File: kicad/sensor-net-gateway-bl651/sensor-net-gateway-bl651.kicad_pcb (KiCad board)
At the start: 2 copper layers, 26 x 56 mm, 41 parts, among them M1 M50-3130545, M2 M50-3130545, SW1 PTS526_SM15_SMTR2_LFS, U1 USB_micro_ab, U2 USBLC6-2SC6, U3 FT230XQ, Y1 32.768 kHz

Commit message: routing snapshot
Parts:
- removed CD1: CORTEX-DEBUG, HH_CNCTech:CORTEX-DEBUG
- added C17: 0.1µF, Capacitor_SMD:C_0603_1608Metric, B.Cu at (154.0, 92.0)
- added L3: logo, HH_Hochreiner:logo, B.Cu at (168.0, 119.0)
- moved LED1 27.3 mm to (174.0, 122.0), turned to 90 degrees
- moved R3 20.7 mm to (173.1, 117.3), turned to 270 degrees
- moved R4 20.4 mm to (174.9, 117.3), turned to 270 degrees
- moved R6 16.8 mm to (159.5, 94.4)
- moved S2 16.6 mm to (154.0, 92.0), turned to 180 degrees
- moved R5 16.0 mm to (159.5, 92.8)
- moved M2 5.60 mm to (156.3, 103.5)
- moved SC1 5.30 mm to (161.4, 87.7)
- moved H2 5.10 mm to (155.0, 85.0)
- moved C14 4.90 mm to (162.4, 96.2)
- moved Y1 4.90 mm to (159.9, 97.8)
- moved BL1 4.81 mm to (169.0, 99.6)
- moved C15 4.80 mm to (156.9, 96.5)
- moved C16 4.80 mm to (156.9, 99.1)
- moved C13 4.64 mm to (172.7, 109.9), turned to 0 degrees
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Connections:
- net Net-(U1-Pad2) renamed /usb/D_N
- net Net-(U1-Pad3) renamed /usb/D_P
- BL1 pad 12: /mcu/FTDI_DIO0 -> /mcu/FTDI_DIO1
- BL1 pad 13: /mcu/FTDI_DIO1 -> /mcu/FTDI_DIO0
- BL1 pad 14: /mcu/FTDI_DIO2 -> /mcu/FTDI_DIO3
- BL1 pad 15: /mcu/FTDI_DIO3 -> /mcu/FTDI_DIO2
- BL1 pad 2: /mcu/SPI_MISO -> /mcu/LED_GREEN
- BL1 pad 21: (no net) -> /mcu/UART2.TX
- BL1 pad 22: (no net) -> /mcu/UART2.RX
- BL1 pad 28: (no net) -> /sensor/SCL
- BL1 pad 3: /mcu/SPI_MOSI -> /mcu/LED_RED
- BL1 pad 30: /sensor/SCL -> /mcu/GPIO_2
- BL1 pad 31: /mcu/LED_GREEN -> /mcu/~SPI_CS
- BL1 pad 32: /mcu/LED_RED -> /mcu/SPI_CLK
- BL1 pad 33: /mcu/GPIO_2 -> /mcu/SPI_MOSI
- BL1 pad 34: /mcu/GPIO_1 -> /mcu/SPI_MISO
- BL1 pad 35: /mcu/~SPI_CS -> /mcu/I2C_SDA
- BL1 pad 37: /mcu/I2C_SDA -> /mcu/GPIO_1
- BL1 pad 38: /mcu/SPI_CLK -> (no net)
- C1 pad 2: /power/GND -> GND
- C10 pad 2: /power/GND -> GND
- C11 pad 2: /power/GND -> GND
- C12 pad 2: /power/GND -> GND
- C2 pad 2: /power/GND -> GND
- C21 pad 2: /power/GND -> GND
- C3 pad 2: /power/GND -> GND
- C4 pad 2: /power/GND -> GND
- C5 pad 2: /power/GND -> GND
- C6 pad 1: /power/GND -> GND
- C7 pad 2: /power/GND -> GND
- C9 pad 2: /power/GND -> GND
- L2 pad 2: /power/GND -> GND
- M2 pad 1: /usb/UART.RX -> /power/3V0
- M2 pad 2: /usb/UART.TX -> /mcu/SWO
- M2 pad 4: /usb/UART.RTS -> /mcu/UART2.TX
- M2 pad 5: /usb/UART.CTS -> /mcu/UART2.RX
- S1 pad 6: /power/GND -> GND
- S1 pad 8: /power/GND -> GND
- S2 pad 4: /power/GND -> GND
- U1 pad 5: /power/GND -> GND
- U2 pad 2: /power/GND -> GND
- U3 pad 13: /power/GND -> GND
- U3 pad 17: /power/GND -> GND
- U3 pad 3: /power/GND -> GND
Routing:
- net /power/3V0: track 0.00 -> 77.7 mm, vias 0 -> 7
- net GND: track 0.00 -> 39.1 mm, vias 0 -> 19
- net /power/VBUS: track 0.00 -> 26.3 mm, vias 0 -> 4
- net /mcu/FTDI_DIO2: track 0.00 -> 21.3 mm, vias 0 -> 2
- net /mcu/GPIO_1: track 0.00 -> 21.3 mm, vias 0 -> 2
- net /usb/UART.CTS: track 0.00 -> 19.7 mm
- net /mcu/I2C_SCL: track 0.00 -> 19.1 mm
- net /mcu/I2C_SDA: track 0.00 -> 17.1 mm
- net /mcu/SWO: track 0.00 -> 17.1 mm, vias 0 -> 2
- net /usb/UART.RX: track 0.00 -> 17.0 mm
- net /mcu/~RESET: track 0.00 -> 14.7 mm, vias 0 -> 1
- net /mcu/FTDI_DIO3: track 0.00 -> 14.1 mm, vias 0 -> 2
- net /mcu/SWDIO: track 0.00 -> 14.1 mm, vias 0 -> 2
- net /usb/UART.RTS: track 0.00 -> 13.0 mm
- net /mcu/FTDI_DIO1: track 0.00 -> 13.0 mm
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- added copper zone on B.Cu, net GND
- added copper zone on F.Cu, net GND
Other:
- board size 26 x 56 mm -> 24 x 50 mm

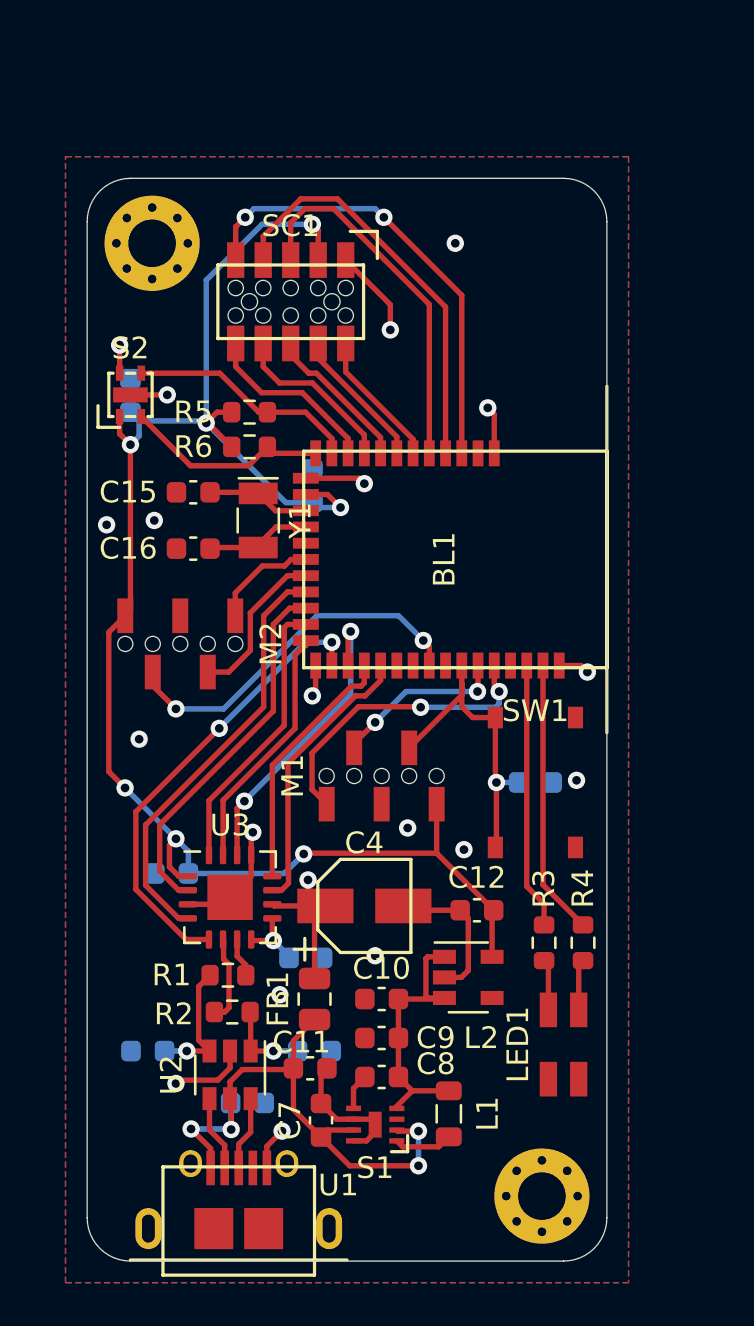
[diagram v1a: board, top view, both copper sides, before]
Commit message: added pin descriptions
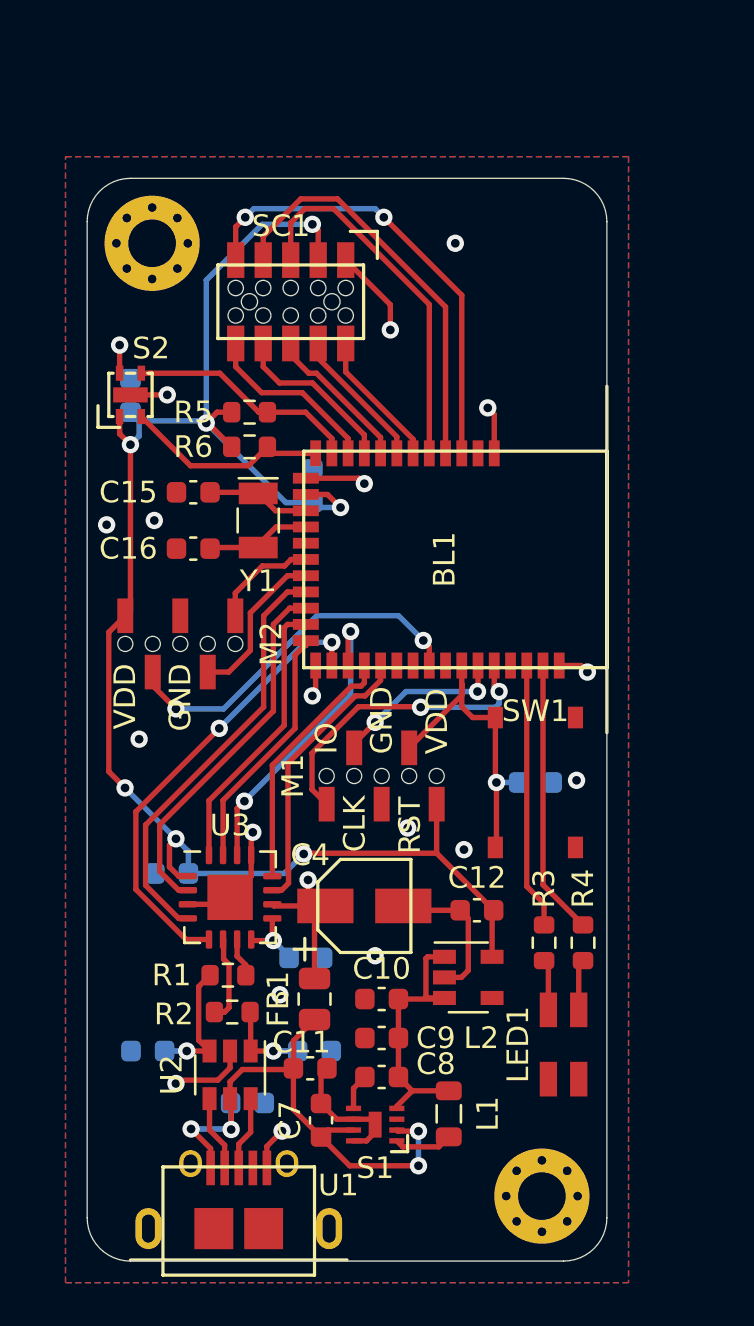
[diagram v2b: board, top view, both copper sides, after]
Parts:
- moved L3 15.7 mm to (161.5, 104.7), turned to 90 degrees
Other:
- board text added: "CLK"
- board text added: "GND"
- board text added: "IO"
- board text added: "RST"
- board text added: "VDD"
- board text added: "sensor-net-gateway-bl651 v1.0.0 hochreiner.net"
